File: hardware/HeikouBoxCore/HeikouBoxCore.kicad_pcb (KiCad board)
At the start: 2 copper layers, 40 x 40 mm, 35 parts, among them J1 L, J2 B, J3 R, J4 T, U1 EP3C25E144

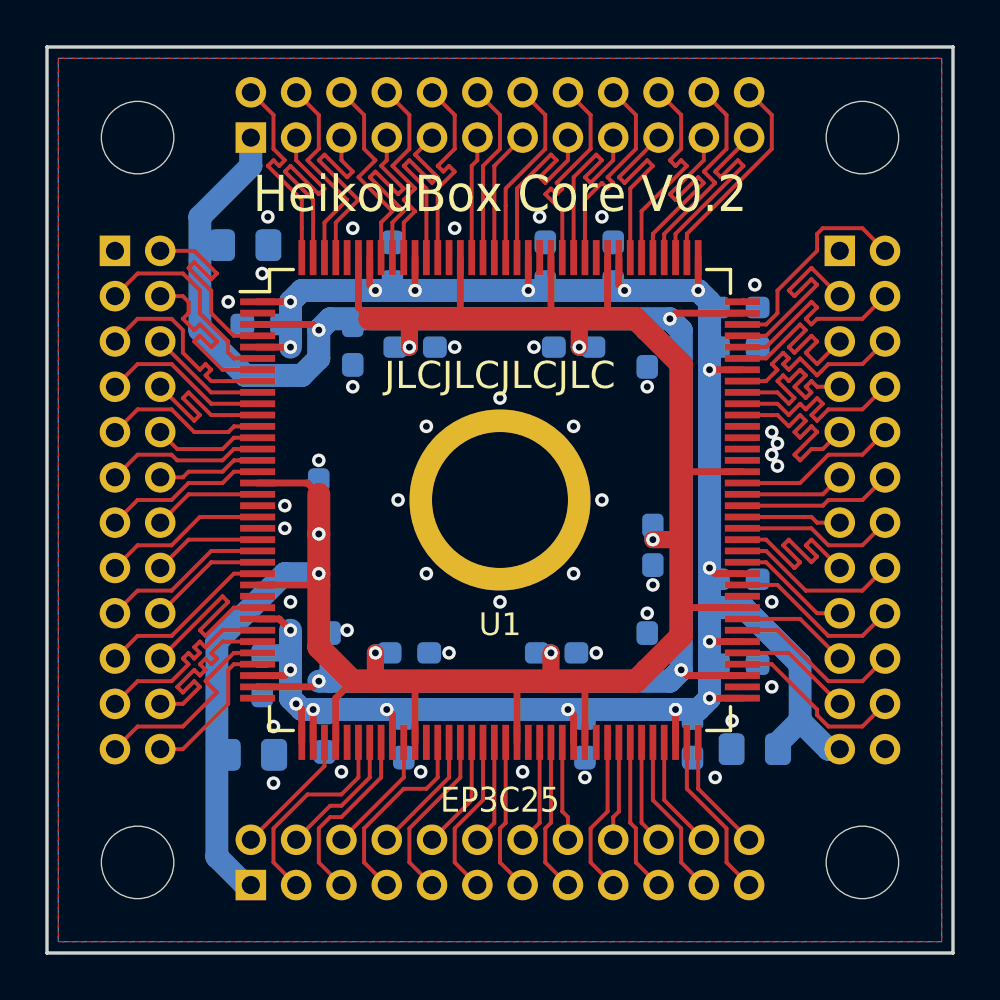
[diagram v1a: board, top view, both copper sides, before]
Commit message: Core: Create/use overall footprint again
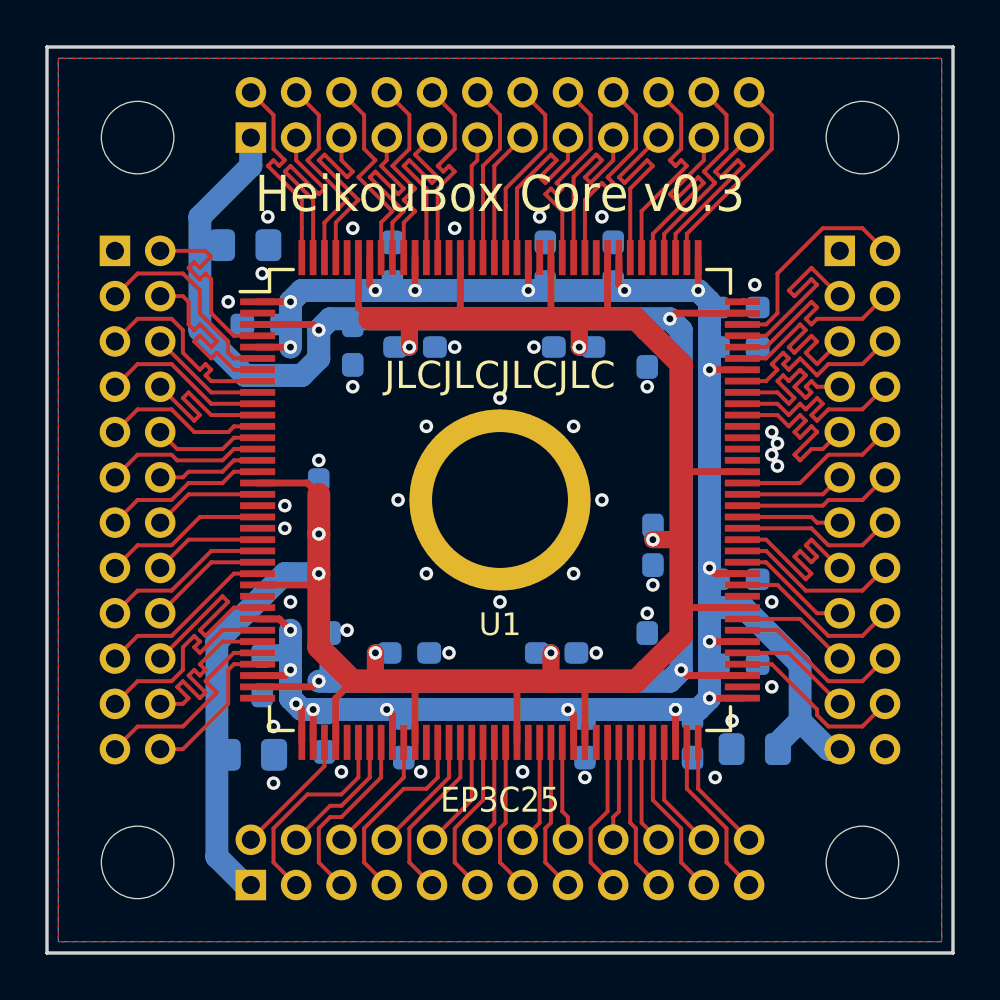
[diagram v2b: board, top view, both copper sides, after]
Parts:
- removed J2: B, KSK_HeikouBox:PinHeader_2x12_P2.00mm_Vertical-MIRRORED
- removed J3: R, KSK_HeikouBox:PinHeader_2x12_P2.00mm_Vertical-MIRRORED
- removed J4: T, KSK_HeikouBox:PinHeader_2x12_P2.00mm_Vertical-MIRRORED
- removed MH1, MH2, MH3, MH4: M3, MountingHole:MountingHole_3.2mm_M3
- J1: value L -> HeikouBox_Core; footprint KSK_HeikouBox:PinHeader_2x12_P2.00mm_Vertical-MIRRORED -> KSK_HeikouBox:HeikouBox-Core-Top; moved to F.Cu
- moved J1 18.6 mm to (37.0, 37.0), turned to 0 degrees
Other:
- board text added: "HeikouBox Core v0.3"
- board text removed: "HeikouBox Core V0.2"

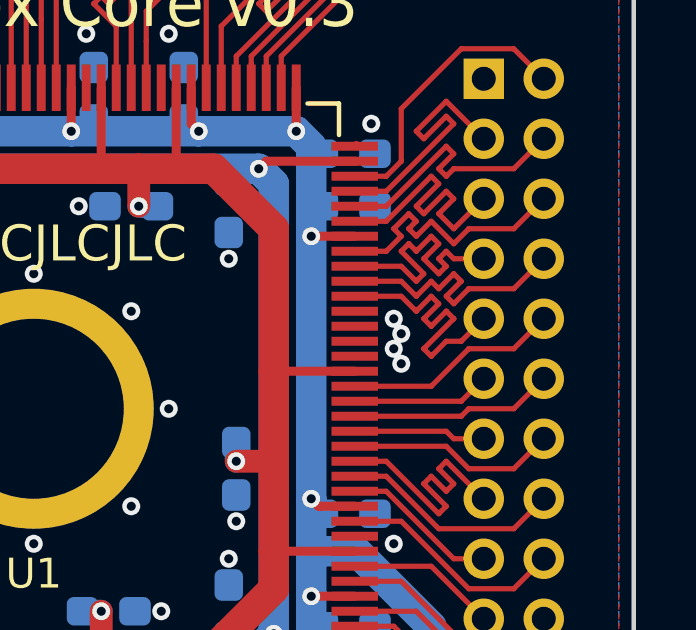
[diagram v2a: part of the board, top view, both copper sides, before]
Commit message: Update components on core
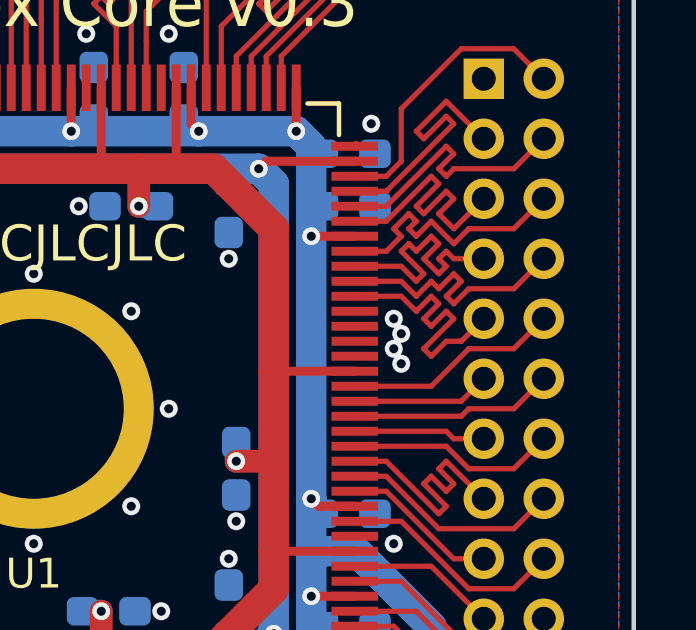
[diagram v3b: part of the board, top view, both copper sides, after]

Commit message: Mostly routed board
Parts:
- J1: value HeikouBox_Core -> HeikouBox-Core-Plug
- U1: footprint KSK_HeikouBox:EQFP-144-HANDSOLDER -> KSK_HeikouBox:LQFP-144-1EP_20x20mm_P0.5mm_EP6.61x6.61mm_HandSoldering
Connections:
- net /V12 renamed /1V2
- net /V25 renamed /2V5
- net /V33 renamed /3V3

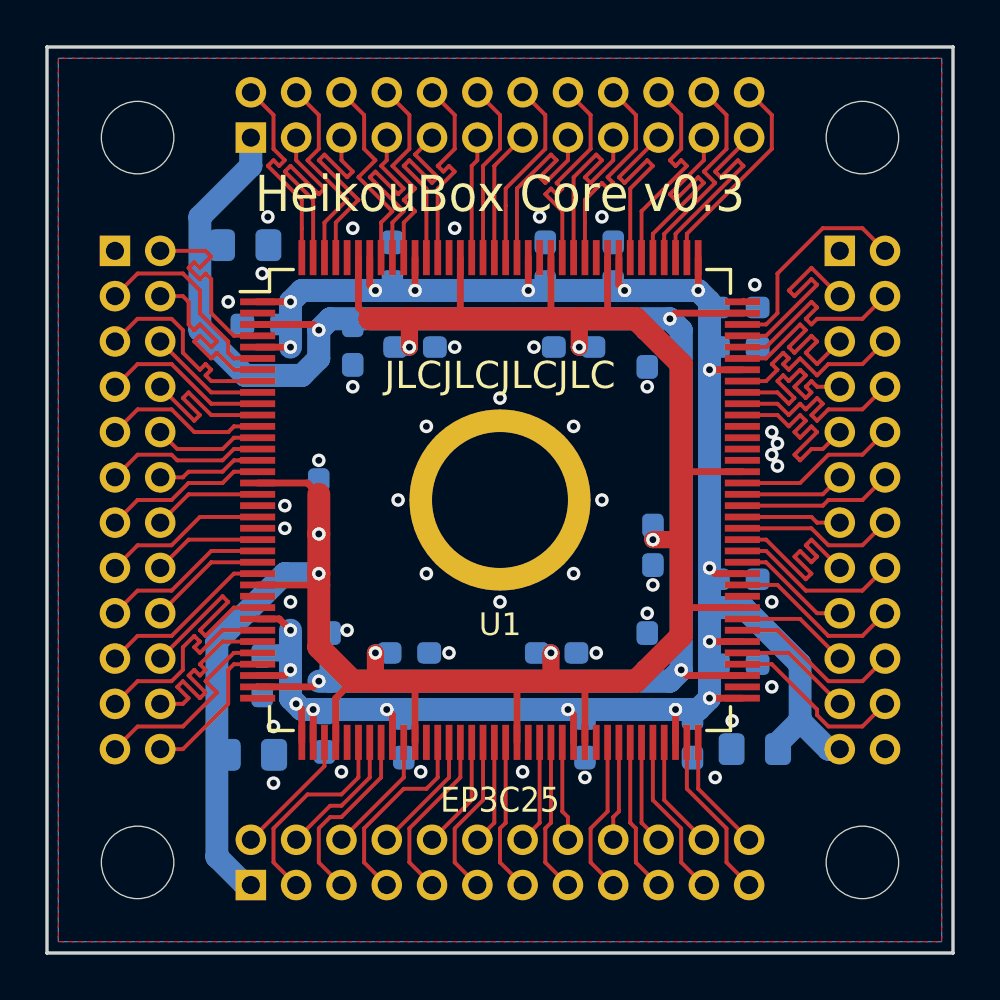
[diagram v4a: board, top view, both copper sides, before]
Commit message: Fix core orientation
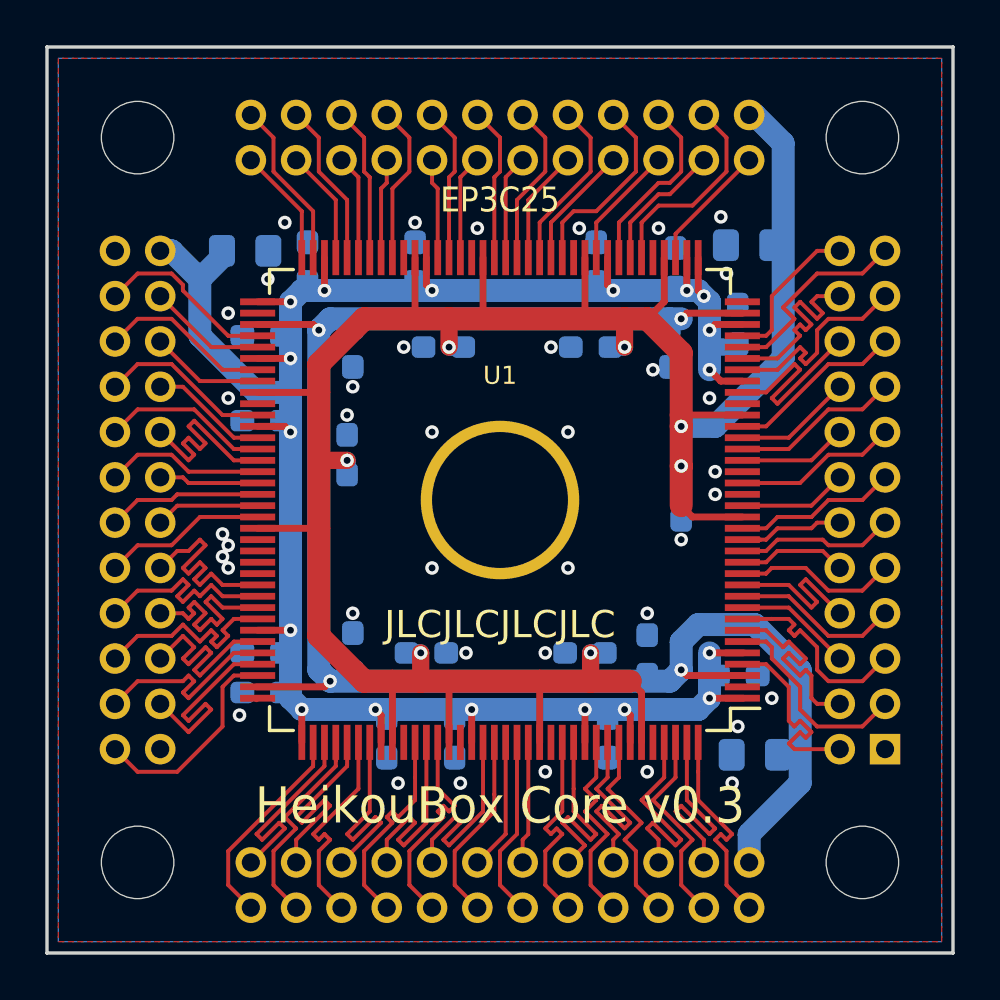
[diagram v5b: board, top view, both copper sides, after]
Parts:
- moved C25 31.8 mm to (48.2, 48.2), turned to 180 degrees
- moved C24 31.5 mm to (48.0, 25.8), turned to 180 degrees
- moved C26 31.5 mm to (25.8, 26.0), turned to 0 degrees
- moved C11 27.0 mm to (26.5, 45.5), turned to 180 degrees
- moved C15 27.0 mm to (28.5, 26.5), turned to 270 degrees
- moved C19 26.1 mm to (47.5, 29.2), turned to 270 degrees
- moved C7 26.1 mm to (47.5, 44.8), turned to 0 degrees
- moved C18 25.7 mm to (44.8, 26.8), turned to 270 degrees
- moved C14 25.5 mm to (26.5, 29.8), turned to 0 degrees
- moved C12 25.0 mm to (26.5, 43.8), turned to 180 degrees
- moved C10 23.3 mm to (32.0, 47.5), turned to 270 degrees
- moved C8 23.0 mm to (41.8, 47.5), turned to 270 degrees
- moved C17 22.7 mm to (41.2, 26.5), turned to 270 degrees
- moved C16 22.3 mm to (33.2, 26.5), turned to 270 degrees
- moved C13 22.1 mm to (26.5, 33.5), turned to 180 degrees
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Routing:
- net /GND: vias 43 -> 39
